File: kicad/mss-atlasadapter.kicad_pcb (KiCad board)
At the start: 2 copper layers, 69.8 x 63.5 mm, 62 parts, among them J1 6P6C, J2 6P6C, J3 Screw_Terminal_01x02, J4 8P8C, Q1 ZXMS6004FF, Q2 ZXMS6004FF, Q3 ZXMS6004FF, U1 AP7381-50Y, U2 AP3012, U3 74HC4049, U4 74HC4049

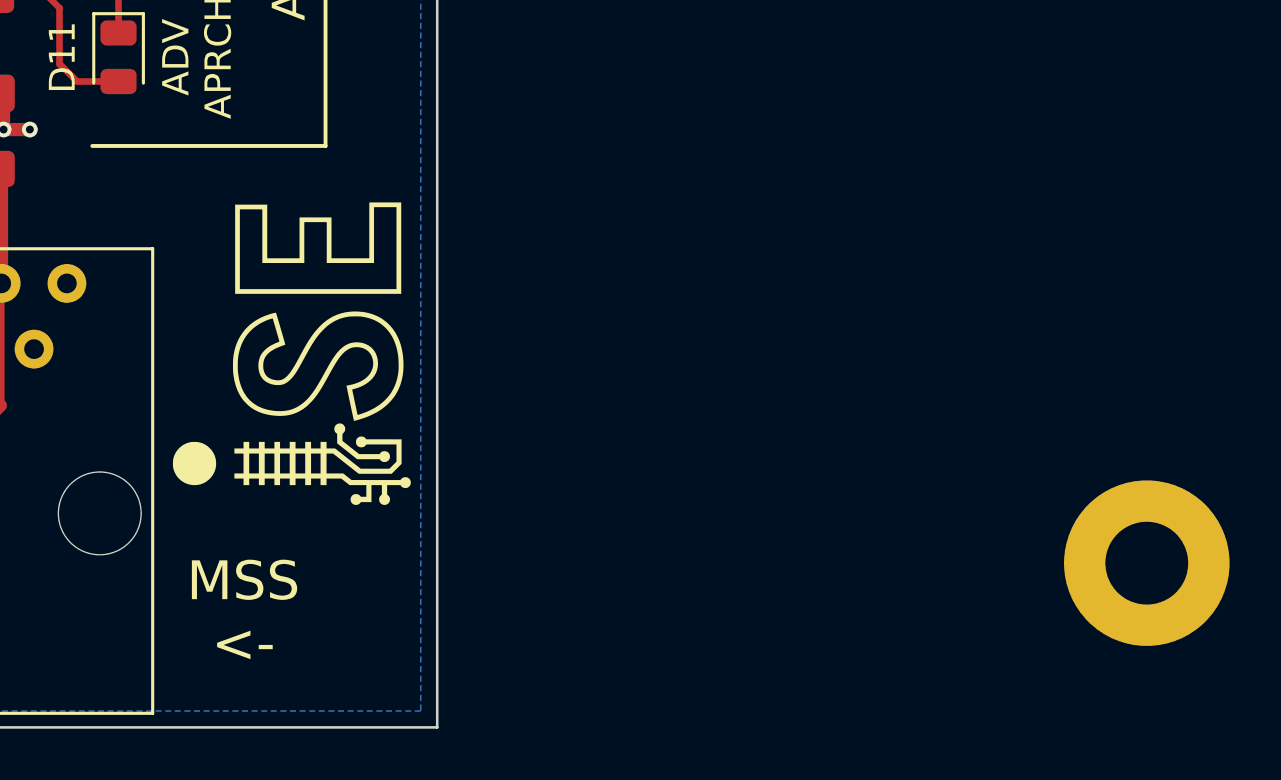
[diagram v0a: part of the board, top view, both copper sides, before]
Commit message: Fix stray hole that didn't get moved
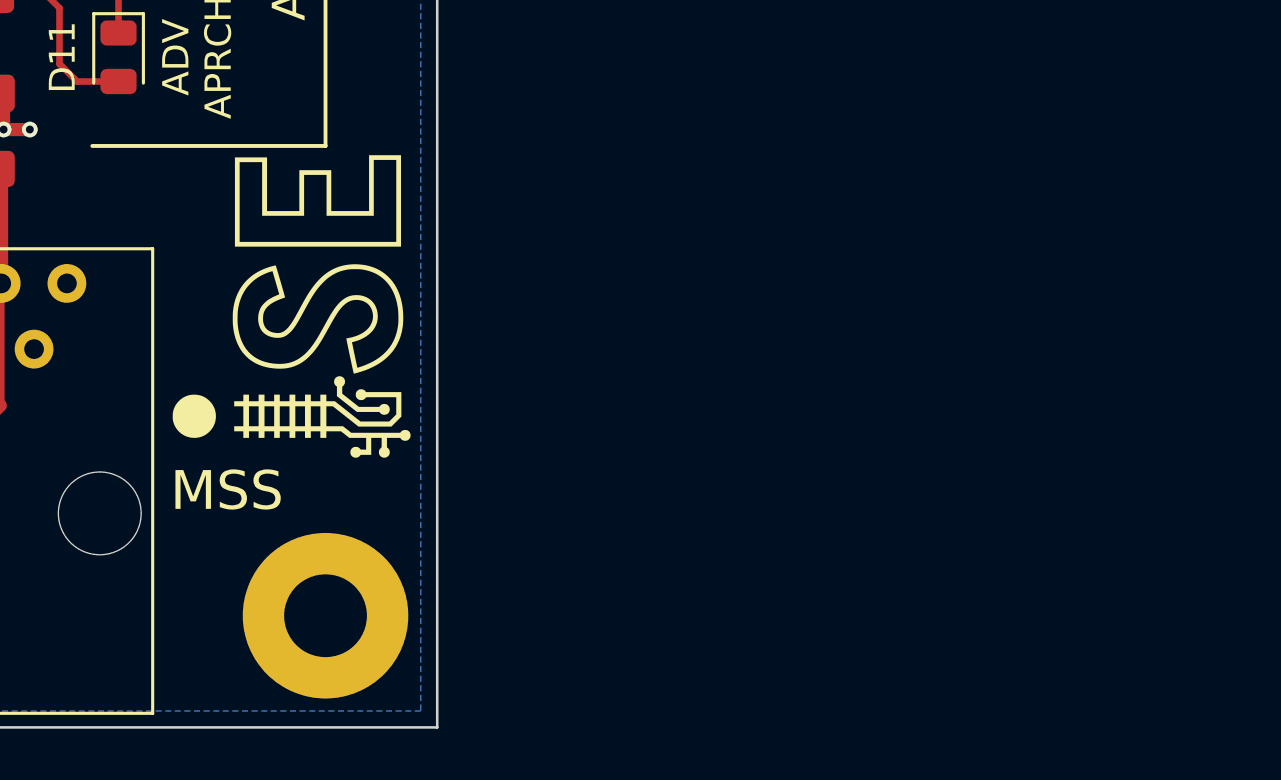
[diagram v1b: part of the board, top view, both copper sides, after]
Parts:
- moved H2 31.8 mm to (90.9, 187.5)
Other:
- board text added: "MSS"
- board text removed: "MSS <-"

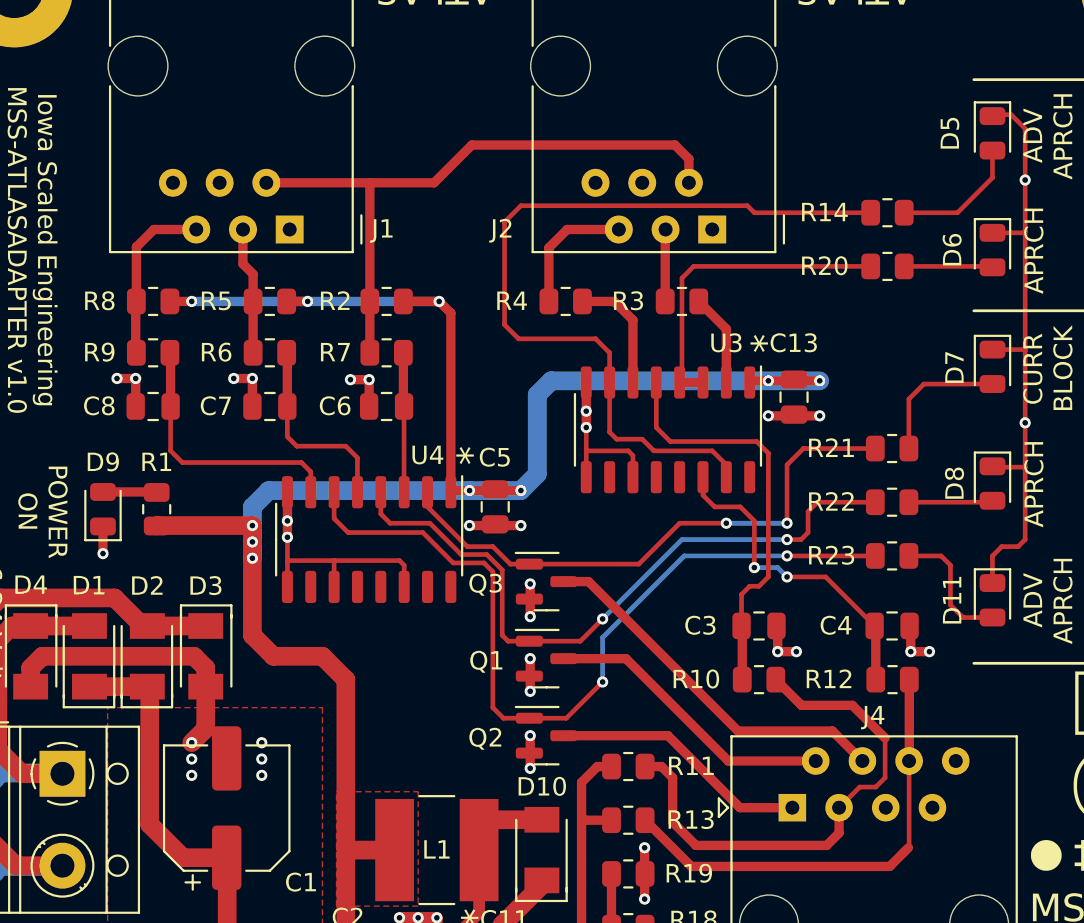
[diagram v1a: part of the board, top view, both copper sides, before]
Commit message: Add test points
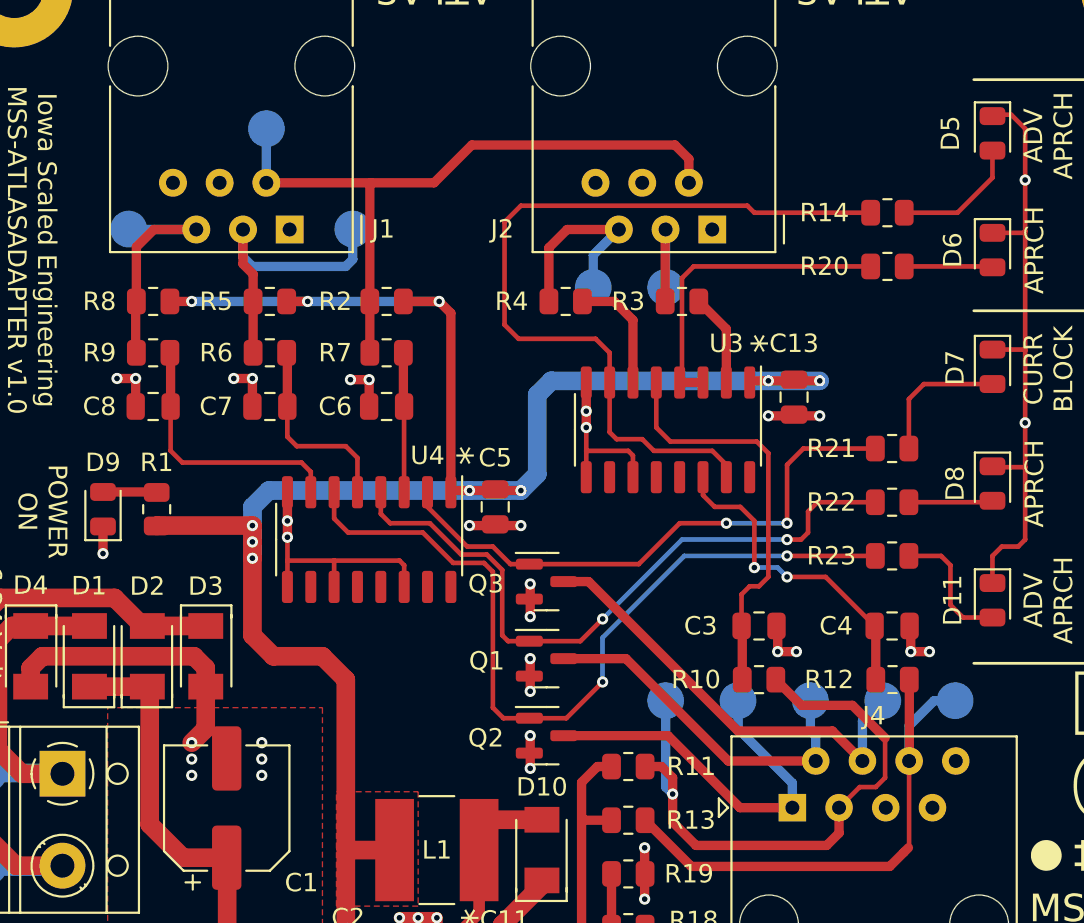
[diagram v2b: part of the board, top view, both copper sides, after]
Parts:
- added TP10: TestPoint, TestPoint:TestPoint_Pad_D2.0mm, B.Cu at (77.0, 171.3)
- added TP11: TestPoint, TestPoint:TestPoint_Pad_D2.0mm, B.Cu at (65.2, 171.3)
- added TP12: TestPoint, TestPoint:TestPoint_Pad_D2.0mm, B.Cu at (80.9, 171.3)
- added TP3: TestPoint, TestPoint:TestPoint_Pad_D2.0mm, B.Cu at (43.4, 140.2)
- added TP4: TestPoint, TestPoint:TestPoint_Pad_D2.0mm, B.Cu at (35.9, 145.7)
- added TP5: TestPoint, TestPoint:TestPoint_Pad_D2.0mm, B.Cu at (61.2, 148.8)
- added TP6: TestPoint, TestPoint:TestPoint_Pad_D2.0mm, B.Cu at (48.1, 145.7)
- added TP7: TestPoint, TestPoint:TestPoint_Pad_D2.0mm, B.Cu at (65.2, 148.8)
- added TP8: TestPoint, TestPoint:TestPoint_Pad_D2.0mm, B.Cu at (69.1, 171.3)
- added TP9: TestPoint, TestPoint:TestPoint_Pad_D2.0mm, B.Cu at (73.0, 171.3)
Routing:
- net Net-(J1-Pad3): track 6.94 -> 16.4 mm
- net Net-(J4-Pad1): track 14.1 -> 21.1 mm
- net Net-(J4-Pad3): track 28.0 -> 33.2 mm, vias 0 -> 1
- net Net-(J4-Pad6): track 25.3 -> 30.3 mm
- net Net-(J4-Pad4): track 20.3 -> 24.0 mm
- net Net-(J2-Pad5): track 7.14 -> 10.9 mm
- net Net-(J1-Pad5): track 9.46 -> 13.1 mm
- net Net-(J4-Pad2): track 16.0 -> 19.4 mm
- net Net-(J2-Pad3): track 3.92 -> 7.08 mm
- net Net-(J1-Pad2): track 34.7 -> 37.7 mm

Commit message: Updates from Michael's review
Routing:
- net +5V: track 119.3 -> 119.8 mm
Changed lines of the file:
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@@
     (effects (font (size 1.016 1.016) (thickness 0.1524)))
   )
-  (gr_text "MSS" (at 87.122 182.626) (layer "F.SilkS")
+  (gr_text "MSS" (at 85.852 185.293 90) (layer "F.SilkS")
     (effects (font (size 1.5 1.5) (thickness 0.3)))
   )
@@
   (segment (start 60.833 154.016) (end 60.833 156.464) (width 0.508) (layer "F.Cu") (net 2))
   (segment (start 82.931 164.9245) (end 82.931 163.449) (width 0.254) (layer "F.Cu") (net 2))
-  (segment (start 44.262 186.624) (end 43.942 186.944) (width 1.016) (layer "F.Cu") (net 2))
   (segment (start 41.656 153.797) (end 42.672 153.797) (width 0.508) (layer "F.Cu") (net 2))
   (segment (start 44.577 162.433) (end 44.577 161.544) (width 0.508) (layer "F.Cu") (net 2))
@@
   (segment (start 84.709 152.273) (end 84.709 145.796) (width 0.254) (layer "F.Cu") (net 2))
   (segment (start 50.673 163.703) (end 50.927 163.957) (width 0.254) (layer "F.Cu") (net 2))
-  (segment (start 48.006 153.8605) (end 49.022 153.8605) (width 0.508) (layer "F.Cu") (net 2))
+  (segment (start 48.006 153.797) (end 49.022 153.797) (width 0.508) (layer "F.Cu") (net 2))
   (segment (start 84.6305 145.8745) (end 84.709 145.796) (width 0.254) (layer "F.Cu") (net 2))
   (segment (start 54.483 161.798) (end 57.277 161.798) (width 0.508) (layer "F.Cu") (net 2))
@@
   (via (at 55.753 188.214) (size 0.6096) (drill 0.3048) (layers "F.Cu" "B.Cu") (free) (net 2))
   (via (at 70.739 155.829) (size 0.6096) (drill 0.3048) (layers "F.Cu" "B.Cu") (net 2))
-  (via (at 49.022 153.8605) (size 0.6096) (drill 0.3048) (layers "F.Cu" "B.Cu") (net 2))
+  (via (at 49.022 153.797) (size 0.6096) (drill 0.3048) (layers "F.Cu" "B.Cu") (net 2))
   (via (at 39.37 173.609) (size 0.6096) (drill 0.3048) (layers "F.Cu" "B.Cu") (free) (net 2))
   (via (at 44.577 162.433) (size 0.6096) (drill 0.3048) (layers "F.Cu" "B.Cu") (net 2))
@@
   (via (at 39.37 175.387) (size 0.6096) (drill 0.3048) (layers "F.Cu" "B.Cu") (free) (net 2))
   (via (at 40.894 186.436) (size 0.6096) (drill 0.3048) (layers "F.Cu" "B.Cu") (free) (net 2))
-  (via (at 48.006 153.8605) (size 0.6096) (drill 0.3048) (layers "F.Cu" "B.Cu") (net 2))
+  (via (at 48.006 153.797) (size 0.6096) (drill 0.3048) (layers "F.Cu" "B.Cu") (net 2))
   (via (at 42.799 189.484) (size 0.6096) (drill 0.3048) (layers "F.Cu" "B.Cu") (free) (net 2))
   (via (at 79.502 168.656) (size 0.6096) (drill 0.3048) (layers "F.Cu" "B.Cu") (net 2))
@@
   (via (at 57.785 170.815) (size 0.6096) (drill 0.3048) (layers "F.Cu" "B.Cu") (free) (net 2))
   (segment (start 37.4885 161.798) (end 37.465 161.8215) (width 1.016) (layer "F.Cu") (net 3))
+  (segment (start 50.9215 186.8115) (end 50.292 186.182) (width 0.508) (layer "F.Cu") (net 3))
   (segment (start 47.752 179.324) (end 47.752 170.18) (width 1.016) (layer "F.Cu") (net 3))
   (segment (start 45.67775 149.606) (end 44.49225 149.606) (width 0.508) (layer "F.Cu") (net 3))
@@
   (segment (start 53.467 159.985) (end 53.559 159.893) (width 0.508) (layer "F.Cu") (net 3))
   (segment (start 51.755 186.8115) (end 53.655 186.8115) (width 0.508) (layer "F.Cu") (net 3))
-  (segment (start 51.755 186.8115) (end 50.6675 186.8115) (width 0.508) (layer "F.Cu") (net 3))
   (segment (start 47.879 179.451) (end 47.752 179.324) (width 1.016) (layer "F.Cu") (net 3))
   (segment (start 46.482 168.91) (end 43.815 168.91) (width 1.016) (layer "F.Cu") (net 3))
   (segment (start 42.672 163.576) (end 42.672 162.687) (width 1.016) (layer "F.Cu") (net 3))
+  (segment (start 49.723 184.724) (end 47.752 184.724) (width 0.508) (layer "F.Cu") (net 3))
   (segment (start 44.299 184.6975) (end 47.2835 184.6975) (width 1.016) (layer "F.Cu") (net 3))
+  (segment (start 50.292 185.293) (end 49.723 184.724) (width 0.508) (layer "F.Cu") (net 3))
   (segment (start 47.752 170.18) (end 46.482 168.91) (width 1.016) (layer "F.Cu") (net 3))
   (segment (start 52.832 149.606) (end 50.8845 149.606) (width 0.508) (layer "F.Cu") (net 3))
   (segment (start 53.559 159.893) (end 57.277 159.893) (width 0.508) (layer "F.Cu") (net 3))
   (segment (start 39.37 149.606) (end 38.1845 149.606) (width 0.508) (layer "F.Cu") (net 3))
-  (segment (start 48.58 184.724) (end 47.752 184.724) (width 0.508) (layer "F.Cu") (net 3))
-  (segment (start 50.6675 186.8115) (end 48.58 184.724) (width 0.508) (layer "F.Cu") (net 3))
+  (segment (start 50.292 186.182) (end 50.292 185.293) (width 0.508) (layer "F.Cu") (net 3))
   (segment (start 50.4063 179.451) (end 47.879 179.451) (width 1.016) (layer "F.Cu") (net 3))
   (segment (start 69.815 153.924) (end 73.533 153.924) (width 0.508) (layer "F.Cu") (net 3))
@@
   (segment (start 42.672 162.687) (end 42.672 161.798) (width 1.016) (layer "F.Cu") (net 3))
   (segment (start 42.672 161.798) (end 37.4885 161.798) (width 1.016) (layer "F.Cu") (net 3))
+  (segment (start 51.755 186.8115) (end 50.9215 186.8115) (width 0.508) (layer "F.Cu") (net 3))
   (via (at 73.533 153.924) (size 0.6096) (drill 0.3048) (layers "F.Cu" "B.Cu") (net 3))
   (via (at 42.672 163.576) (size 0.6096) (drill 0.3048) (layers "F.Cu" "B.Cu") (net 3))
